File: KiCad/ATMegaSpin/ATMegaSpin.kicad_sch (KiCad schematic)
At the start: 23 parts, among them X1 ED281DT

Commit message: Update KiCad files
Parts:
- added B1, B2: BS-7, BS_7:BS-7_MPD, symbol BS_7:BS-7
- added C1, C2: K220J15C0GF5TL2, K220J15C0GF5TL2:CAP_K-SERIES_15-L2_VIS, symbol K220J15C0GF5TL2:K220J15C0GF5TL2
- added Y1: ECS-160-18-4X-CKM, ECS_160_18_4X_CKM:XTAL_ECS-160-18-4X-CKM, symbol ECS-160-18-4X-CKM:ECS-160-18-4X-CKM
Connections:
- net GND: now also B2.1, C1.2, C2.1
- net at X1.10: now also C1.1, Y1.2
- net at S1.1, X1.7: now also B1.2
- net at X1.9: now also C2.2, Y1.1
- new net: B1.1, B2.2

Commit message: Adapt tree
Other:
- company: (none) -> MushuDG-Electronic
- title: (none) -> ATMegaSpin
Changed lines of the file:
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@@
 (kicad_sch (version 20230121) (generator eeschema)
   (paper "A4")
+  (title_block
+    (title "ATMegaSpin")
+    (date "2023-11-15")
+    (rev "1")
+    (company "MushuDG-Electronic")
+  )
   (junction (at 114.3 166.37) (diameter 0) (color 0 0 0 0)
   )

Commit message: Kicad updated
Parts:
- added SW1: MFS101D-6-Z, Library:MFS101D-6-Z_NDC, symbol MFS101D_6_Z:MFS101D-6-Z
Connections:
- net GND: now also SW1.3
- net at S1.1, X1.7: now also SW1.2; no longer B1.2
- new net: B1.2, SW1.1
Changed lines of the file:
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@@
   (junction (at 241.3 50.8) (diameter 0) (color 0 0 0 0)
   )
+  (junction (at 36.83 127) (diameter 0) (color 0 0 0 0)
+  )
   (junction (at 241.3 76.2) (diameter 0) (color 0 0 0 0)
   )
@@
     (stroke (width 0) (type default))
   )
+  (wire (pts (xy 36.83 127) (xy 36.83 135.89))
+    (stroke (width 0) (type default))
+  )
+  (wire (pts (xy 36.83 161.29) (xy 36.83 172.72))
+    (stroke (width 0) (type default))
+  )
   (wire (pts (xy 52.07 83.82) (xy 46.99 83.82))
     (stroke (width 0) (type default))
@@
     (stroke (width 0) (type default))
   )
+  (wire (pts (xy 39.37 88.9) (xy 39.37 135.89))
+    (stroke (width 0) (type default))
+  )
   (wire (pts (xy 36.83 29.21) (xy 123.19 29.21))
     (stroke (width 0) (type default))
@@
     (stroke (width 0) (type default))
   )
-  (wire (pts (xy 88.9 127) (xy 29.21 127))
+  (wire (pts (xy 88.9 127) (xy 36.83 127))
     (stroke (width 0) (type default))
   )
@@
     (stroke (width 0) (type default))
   )
-  (wire (pts (xy 39.37 172.72) (xy 41.91 172.72))
+  (wire (pts (xy 36.83 172.72) (xy 41.91 172.72))
     (stroke (width 0) (type default))
   )
@@
     (stroke (width 0) (type default))
   )
-  (wire (pts (xy 39.37 88.9) (xy 39.37 172.72))
-    (stroke (width 0) (type default))
-  )
   (wire (pts (xy 88.9 88.9) (xy 88.9 127))
+    (stroke (width 0) (type default))
+  )
+  (wire (pts (xy 36.83 127) (xy 29.21 127))
     (stroke (width 0) (type default))
   )
@@
         )
       )
+    )
+  )
+  (symbol (lib_id "MFS101D_6_Z:MFS101D-6-Z") (at 36.83 161.29 90) (unit 1)
+    (in_bom yes) (on_board yes) (dnp no) (fields_autoplaced)
+    (property "Reference" "SW1" (at 43.18 147.32 90)
+      (effects (font (size 1.524 1.524)) (justify right))
+    )
+    (property "Value" "MFS101D-6-Z" (at 43.18 149.86 90)
+      (effects (font (size 1.524 1.524)) (justify right))
+    )
+    (property "Footprint" "Library:MFS101D-6-Z_NDC" (at 36.83 161.29 0)
+      (effects (font (size 1.27 1.27) italic) hide)
+    )
+    (property "Datasheet" "MFS101D-6-Z" (at 36.83 161.29 0)
+      (effects (font (size 1.27 1.27) italic) hide)
+    )
+    (pin "1")
+    (pin "2")
+    (pin "3")
+    (instances
+      (project "ATMegaSpin"
+        (path "/6a02c6cd-0b2e-42ae-a83a-0c87e673bf0b"
+          (reference "SW1") (unit 1)
+        )
+      )

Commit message: Update files
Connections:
- net at X1.2: no longer R1.1
- net at X1.4: now also R1.1
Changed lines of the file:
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@@
+    (stroke (width 0) (type default))
+  )
+  (wire (pts (xy 48.26 81.28) (xy 48.26 25.4))
     (stroke (width 0) (type default))
   )
@@
     (stroke (width 0) (type default))
   )
-  (wire (pts (xy 50.8 25.4) (xy 127 25.4))
+  (wire (pts (xy 48.26 25.4) (xy 127 25.4))
     (stroke (width 0) (type default))
   )
@@
     (stroke (width 0) (type default))
   )
-  (wire (pts (xy 52.07 76.2) (xy 50.8 76.2))
-    (stroke (width 0) (type default))
-  )
   (wire (pts (xy 72.39 88.9) (xy 88.9 88.9))
     (stroke (width 0) (type default))
@@
     (stroke (width 0) (type default))
   )
-  (wire (pts (xy 50.8 25.4) (xy 50.8 76.2))
-    (stroke (width 0) (type default))
-  )
   (wire (pts (xy 238.76 76.2) (xy 241.3 76.2))
     (stroke (width 0) (type default))
   )
+  (wire (pts (xy 52.07 81.28) (xy 48.26 81.28))
+    (stroke (width 0) (type default))
+  )

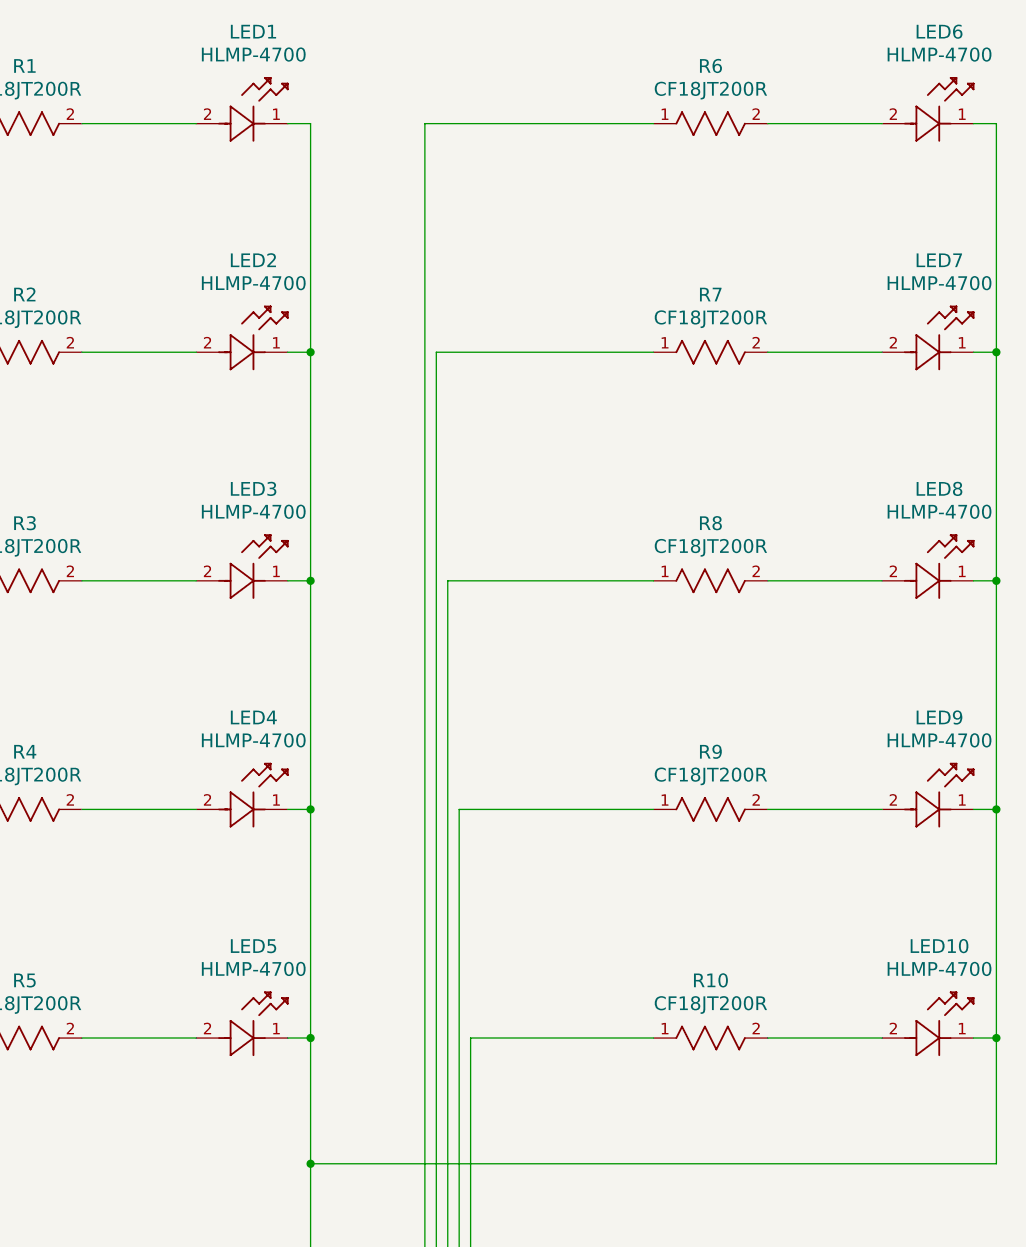
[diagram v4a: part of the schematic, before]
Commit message: Update 3D View + schematic + GERBER files
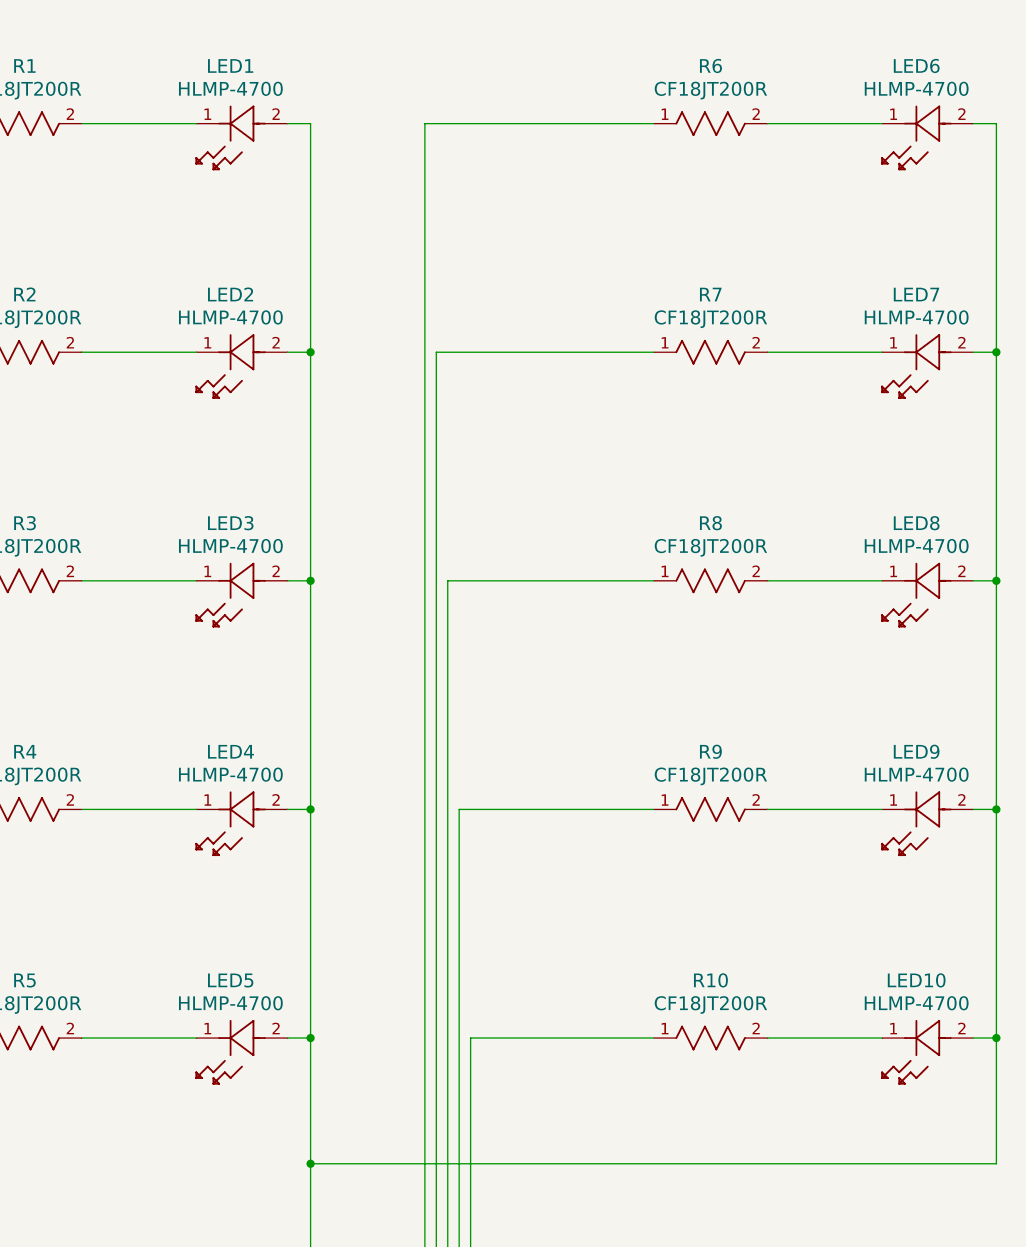
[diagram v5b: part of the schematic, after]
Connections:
- net GND: now also LED1.2, LED10.2, LED2.2, LED3.2, LED4.2, LED5.2, LED6.2, LED7.2, LED8.2, LED9.2; no longer LED1.1, LED10.1, LED2.1, LED3.1, LED4.1, LED5.1, LED6.1, LED7.1, LED8.1, LED9.1
- net at R10.2: now also LED10.1; no longer LED10.2
- net at R2.2: now also LED2.1; no longer LED2.2
- net at R7.2: now also LED7.1; no longer LED7.2
- net at R5.2: now also LED5.1; no longer LED5.2
- net at R3.2: now also LED3.1; no longer LED3.2
- net at R9.2: now also LED9.1; no longer LED9.2
- net at R1.2: now also LED1.1; no longer LED1.2
- net at R6.2: now also LED6.1; no longer LED6.2
- net at R4.2: now also LED4.1; no longer LED4.2
- net at R8.2: now also LED8.1; no longer LED8.2
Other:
- moved on the sheet: LED1, LED10, LED2, LED3, LED4, LED5, LED6, LED7, LED8, LED9
